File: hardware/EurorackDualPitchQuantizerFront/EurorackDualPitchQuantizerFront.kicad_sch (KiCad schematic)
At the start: 67 parts, among them J1 Conn_01x12_Male, J10 Conn_01x04_Male, J11 AudioJack2, J12 AudioJack2, J13 Conn_01x02_Male, J2 Conn_01x01_Male, J3 Conn_01x02_Male, J4 Conn_01x02_Male, J5 AudioJack2, J6 AudioJack2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

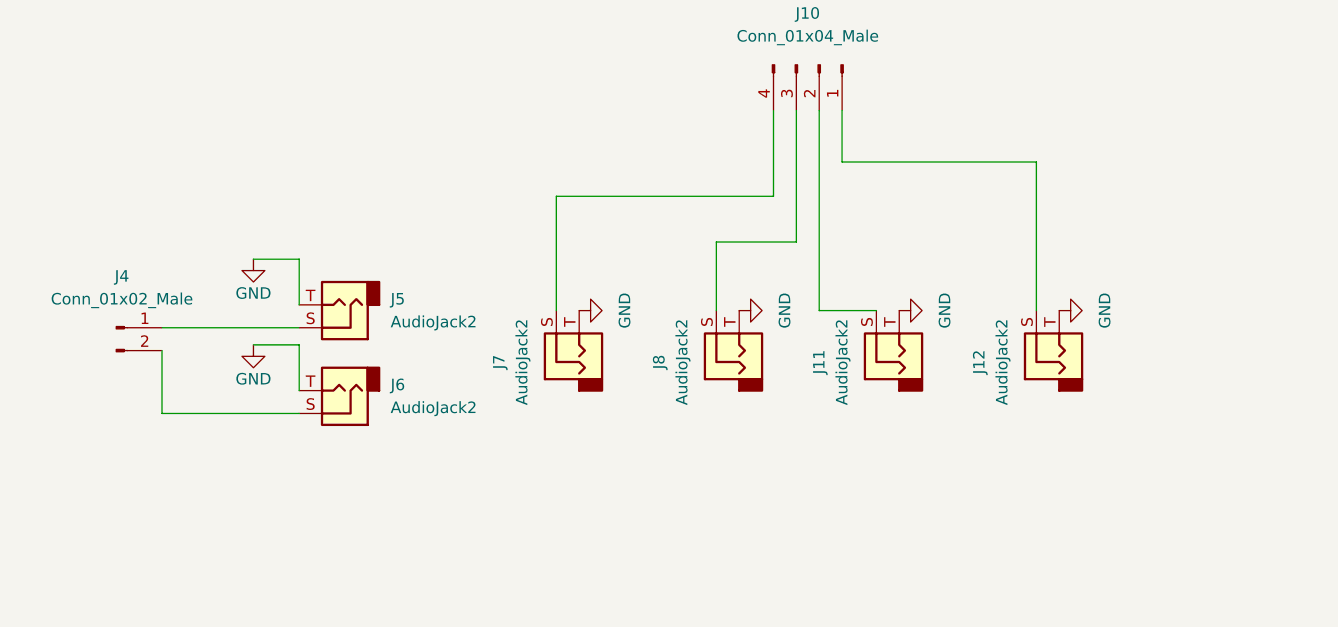
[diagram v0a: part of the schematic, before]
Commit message: made another version that is not viable since it is too tall
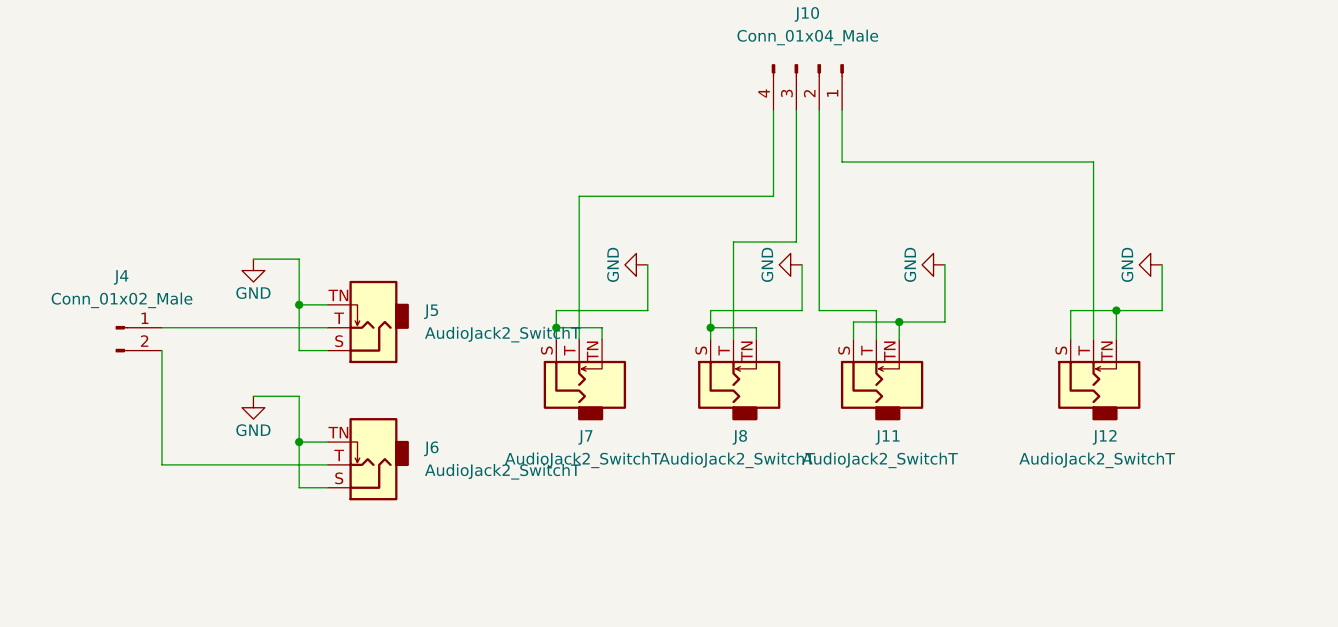
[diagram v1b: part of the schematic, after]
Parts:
- removed J11, J12, J5, J6, J7, J8: AudioJack2, Eurorack:Thonkiconn, symbol Connector:AudioJack2
- added J11, J12, J5, J6, J7, J8: AudioJack2_SwitchT, Eurorack:Thonkiconn, symbol Connector:AudioJack2_SwitchT
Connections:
- net GND: now also J11.S, J11.TN, J12.S, J12.TN, J5.S, J5.TN, J6.S, J6.TN, J7.S, J7.TN, J8.S, J8.TN
- net at J10.1 (Pin_1): now also J12.T
- net at J10.2 (Pin_2): now also J11.T
- net at J10.3 (Pin_3): now also J8.T
- net at J10.4 (Pin_4): now also J7.T
- net at J4.2 (Pin_2): now also J6.T
- net at J4.1 (Pin_1): now also J5.T

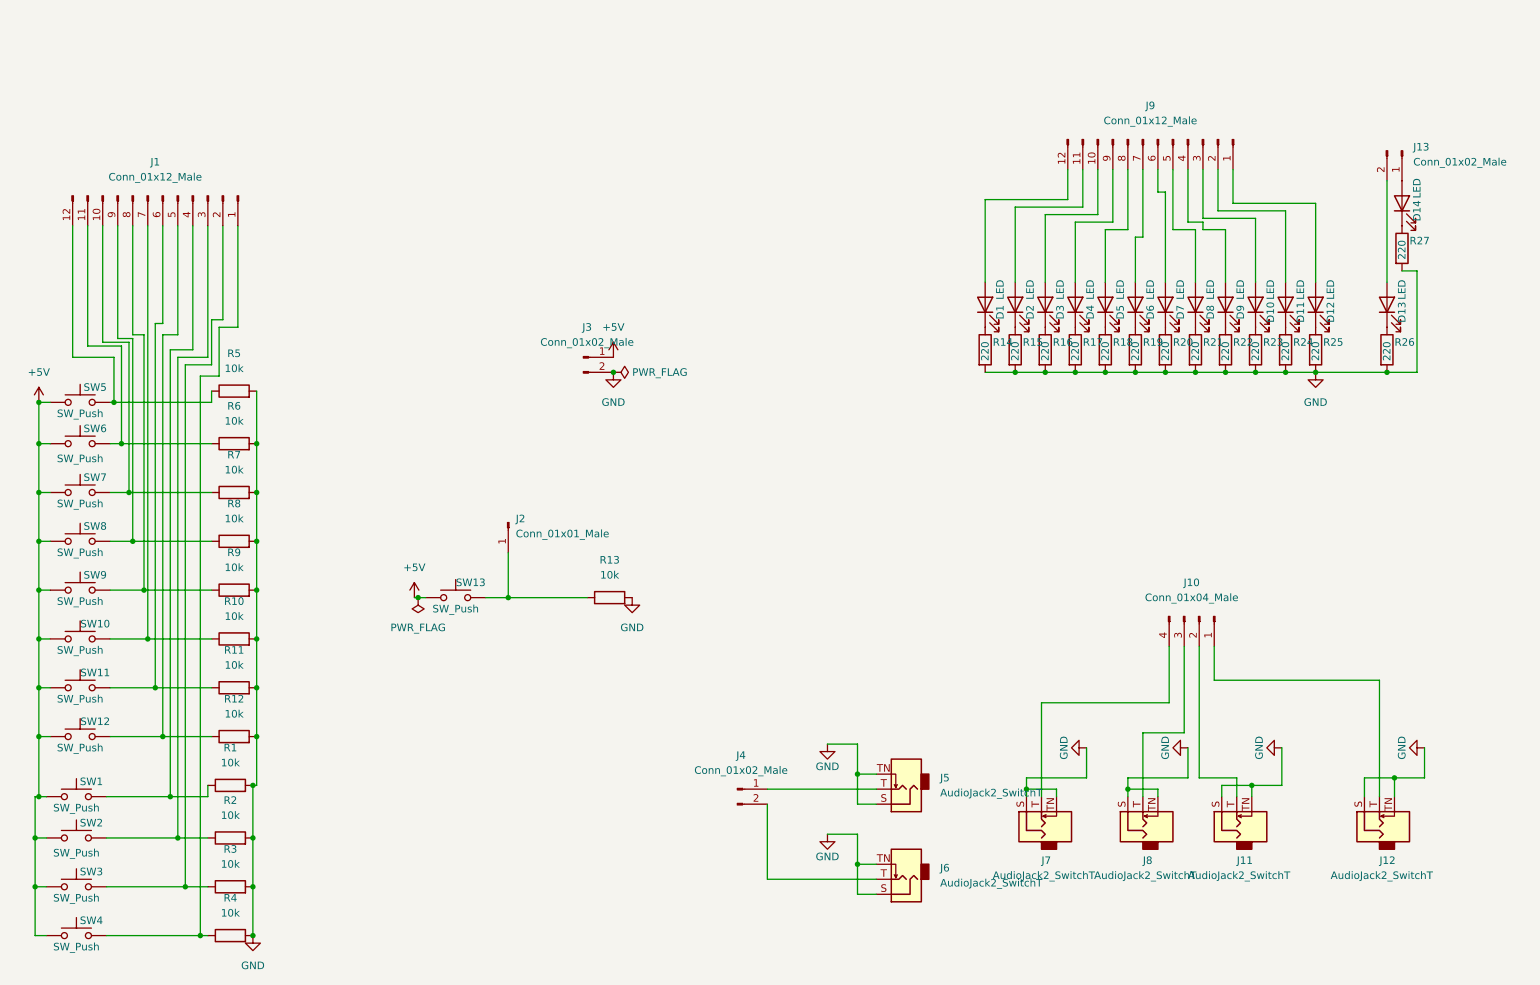
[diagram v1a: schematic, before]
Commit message: Got Rev 1.2 complete. It should be manufacturable and fit into eurorack standards.
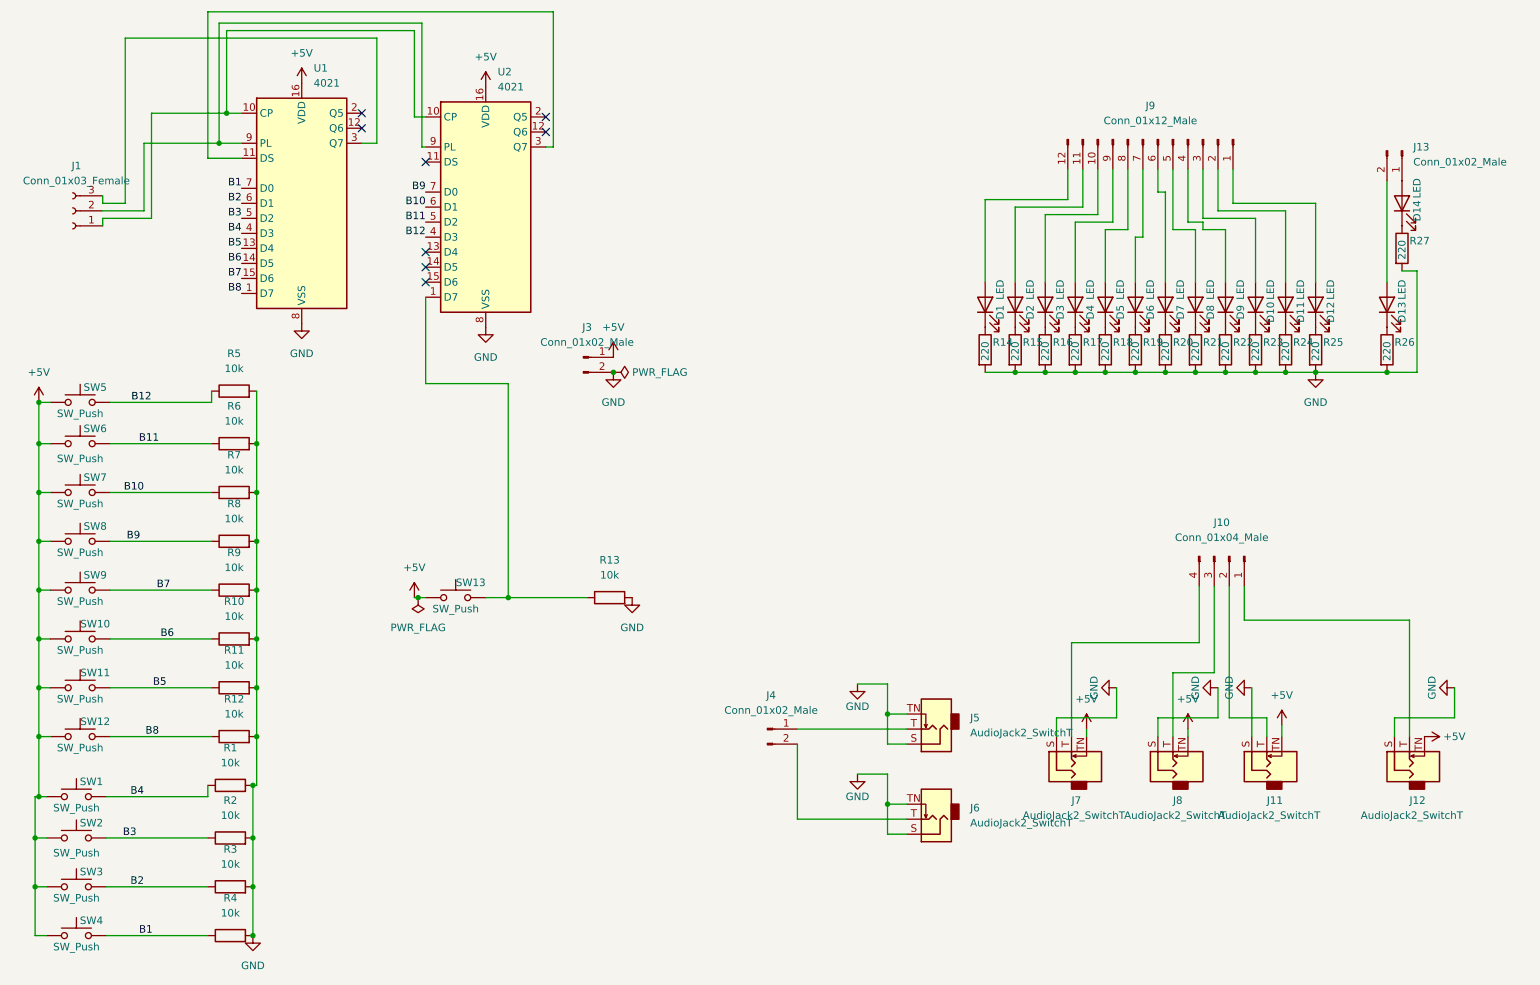
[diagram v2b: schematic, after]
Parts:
- removed J1: Conn_01x12_Male, Connector_PinHeader_2.54mm:PinHeader_1x12_P2.54mm_Vertical, symbol Connector:Conn_01x12_Male
- removed J2: Conn_01x01_Male, Connector_PinHeader_2.54mm:PinHeader_1x01_P2.54mm_Vertical, symbol Connector:Conn_01x01_Male
- added J1: Conn_01x03_Female, Connector_PinHeader_2.54mm:PinHeader_1x03_P2.54mm_Vertical, symbol Connector:Conn_01x03_Female
- added U1, U2: 4021, Package_DIP:DIP-16_W7.62mm_Socket, symbol 4xxx:4021
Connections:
- net +5V: now also J11.TN, J12.TN, J7.TN, J8.TN, U1.16 (VDD), U2.16 (VDD)
- net GND: now also U1.8 (VSS), U2.8 (VSS); no longer J11.TN, J12.TN, J7.TN, J8.TN
- net at R13.1, SW13.2: now also U2.1 (D7)
- net B10: now reaches R7.1, SW7.2
- net B10: now also U2.6 (D1)
- net B3: now reaches R2.1, SW2.2
- net B3: now also U1.5 (D2)
- net B2: now reaches R3.1, SW3.2
- net B2: now also U1.6 (D1)
- net B4: now reaches R1.1, SW1.2
- net B4: now also U1.4 (D3)
- net B5: now reaches R11.1, SW11.2
- net B5: now also U1.13 (D4)
- net B8: now reaches R12.1, SW12.2
- net B8: now also U1.1 (D7)
- net B6: now reaches R10.1, SW10.2
- net B6: now also U1.14 (D5)
- net B1: now reaches R4.1, SW4.2
- net B1: now also U1.7 (D0)
- net B7: now reaches R9.1, SW9.2
- net B7: now also U1.15 (D6)
- net B11: now reaches R6.1, SW6.2
- net B11: now also U2.5 (D2)
- net B12: now reaches R5.1, SW5.2
- net B12: now also U2.4 (D3)
- net B9: now reaches R8.1, SW8.2
- net B9: now also U2.7 (D0)
- new net: J1.1 (Pin_1), U1.10 (CP), U2.10 (CP)
- new net: J1.2 (Pin_2), U1.9 (PL), U2.9 (PL)
- new net: J1.3 (Pin_3), U1.3 (Q7)
- new net: U1.11 (DS), U2.3 (Q7)
- no-connect marks 0 -> 8
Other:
- company: (none) -> Ilmari Hirvonen
- title: (none) -> Dual pitch quantizer front pcb
- moved on the sheet: J10, J11, J12, J4, J5, J6, J7, J8
